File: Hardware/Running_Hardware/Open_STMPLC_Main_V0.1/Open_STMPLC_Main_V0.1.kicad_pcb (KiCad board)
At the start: 2 copper layers, 168.8 x 90 mm, 171 parts, among them J1 Conn_02x08_Odd_Even, J10 10144518-041802LF, J12 USB C, J13 RJ45_Hanrun_HR911105A_Horizon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, J2 USB C, J3 Conn_01x04, J4 TF-01A, J5 Conn_Coaxial, J6 Conn_Coaxial, J7 Simcard_Nano, J8 10144518-041802LF, J9 10144518-041802LF, Q1 DTC143Z, Q2 DTC143Z, Q3 DTC143Z, Q4 DTC143Z, Q5 DTC143Z, Q6 DTC143Z, Q7 DTC143Z, SW1 Switch_6x6, SW2 SW_SPDT, SW3 Switch_6x6, U1 STM32F407IGTx, U10 AP63205WU, U2 ADM2587E, U3 TPS3430WDRC, U4 CH340C, U5 AMS1117-3.3, U6 W25Q64JVSSIQ, U7 LAN8720A, U8 EC200U, U9 AP63200WU, Y1 48MHz, Y2 32.768kHz, Y3 25MHz

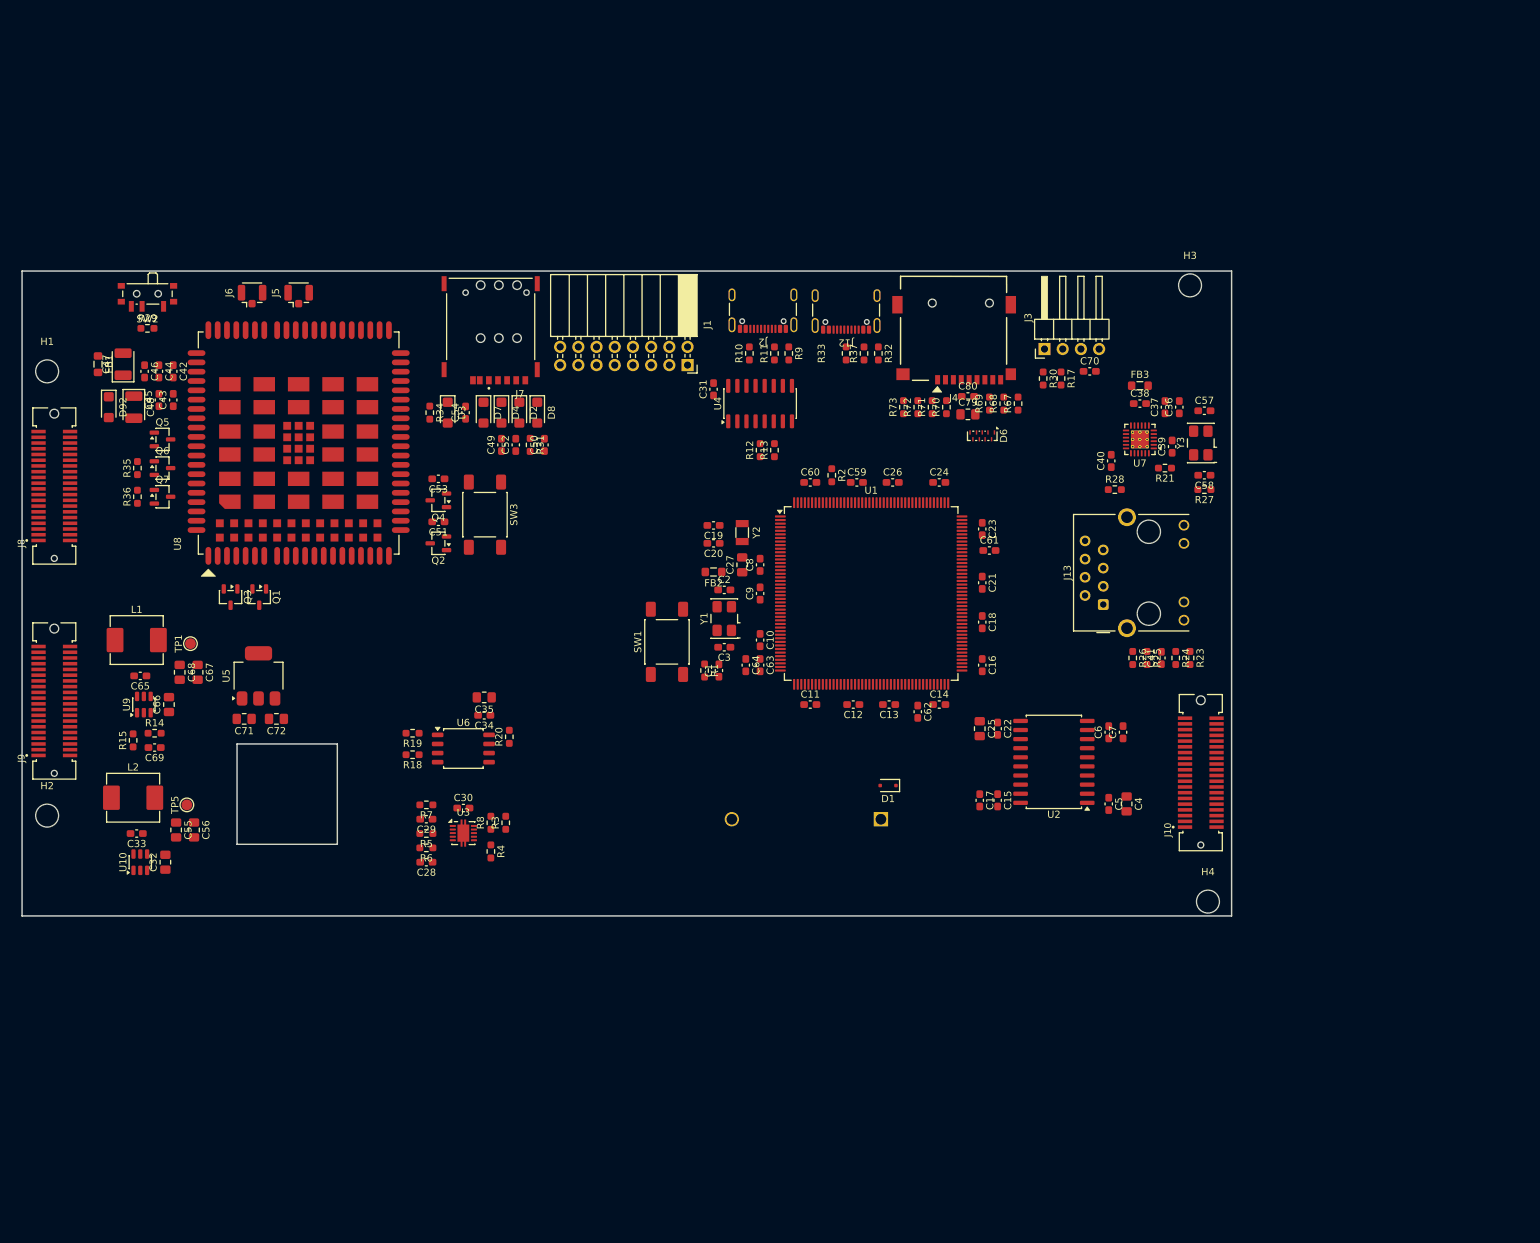
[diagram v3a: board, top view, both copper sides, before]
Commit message: Layer stack up main PCB and pin mapping
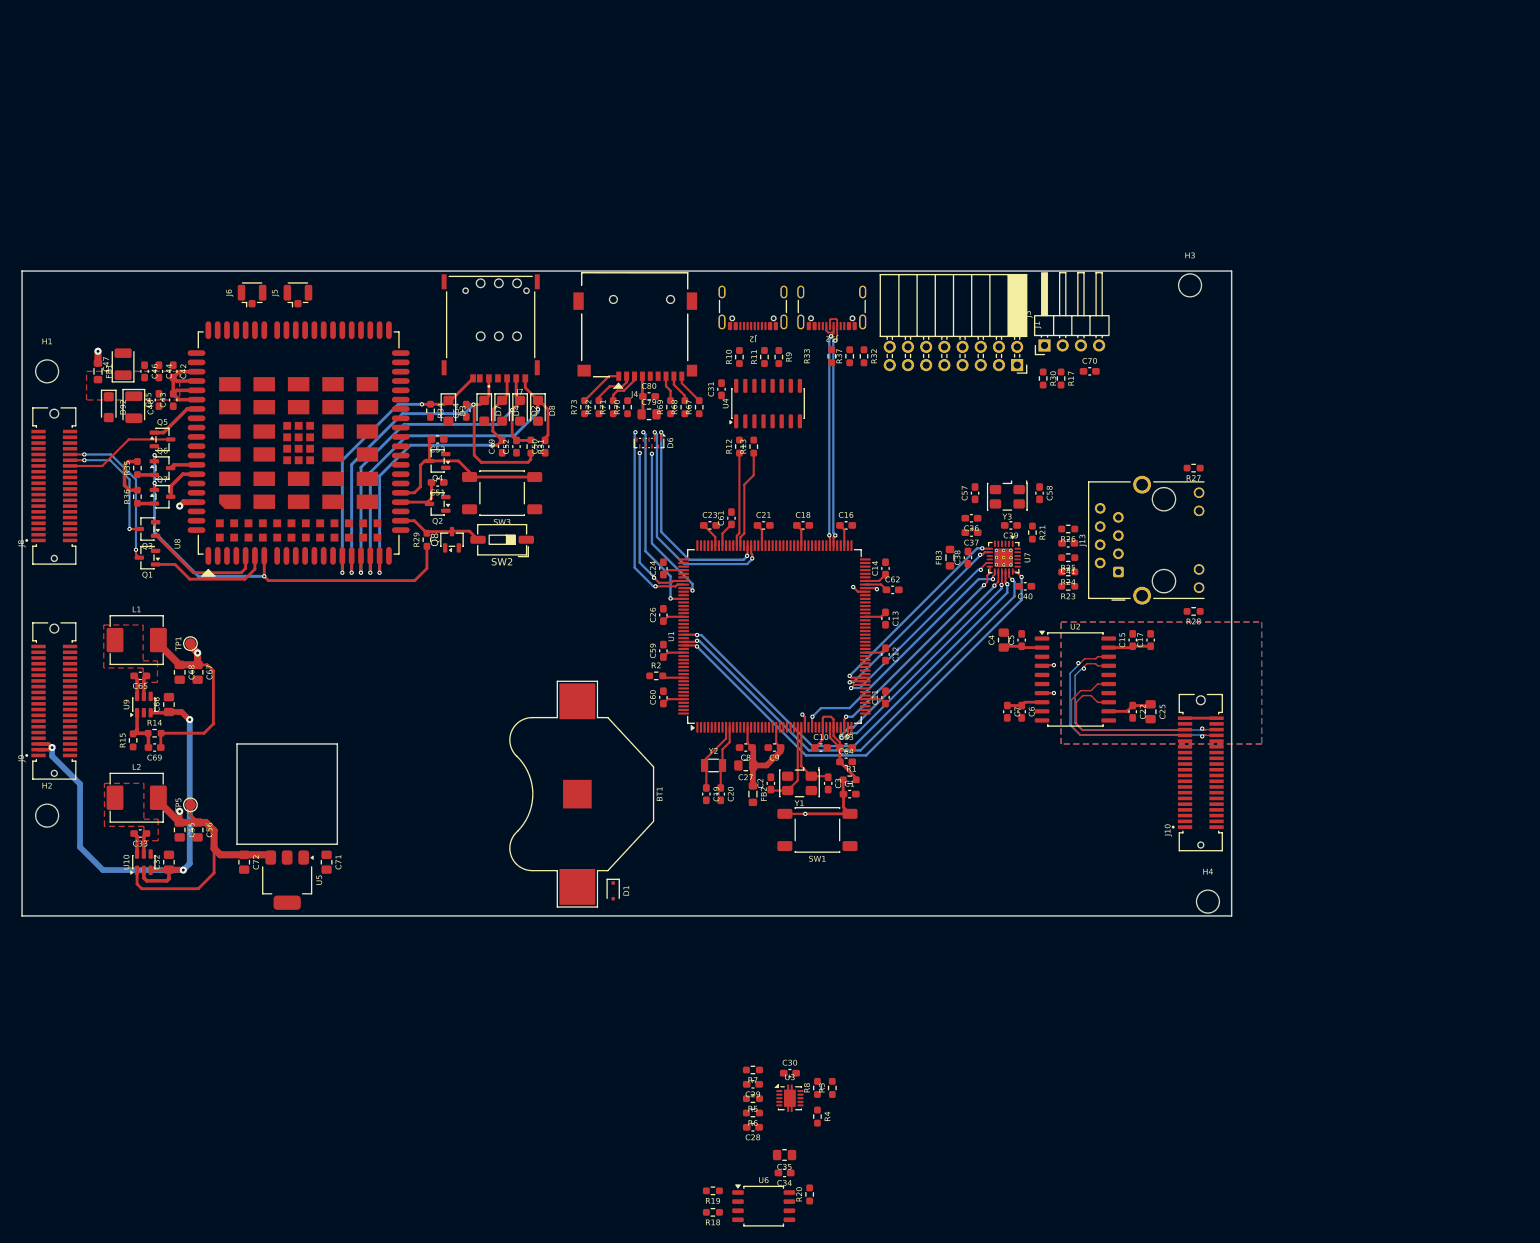
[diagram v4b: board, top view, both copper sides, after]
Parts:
- added Q8: DTC143Z, Package_TO_SOT_SMD:SOT-23-3, F.Cu at (110.0, 87.5)
- BT1: footprint Battery:BatteryHolder_MYOUNG_BS-07-A1BJ001_CR2032 -> Battery:BatteryHolder_Multicomp_BC-2001_1x2032; moved to F.Cu
- SW2: value SW_SPDT -> SW_DIP_x01; footprint Button_Switch_SMD:SW_SPDT_PCM12 -> Button_Switch_SMD:SW_DIP_SPSTx01_Slide_6.7x4.1mm_W6.73mm_P2.54mm_LowProfile_JPin
- moved C34 76.4 mm to (156.4, 175.9)
- moved C35 76.4 mm to (156.4, 173.4)
- moved R18 76.4 mm to (146.4, 181.4)
- moved R19 76.4 mm to (146.4, 178.4)
- moved R20 76.4 mm to (159.9, 178.9)
- moved U6 76.4 mm to (153.5, 180.5)
- moved SW2 60.1 mm to (117.0, 87.5)
- moved C28 58.7 mm to (152.0, 169.5)
- moved C29 58.7 mm to (152.0, 163.5)
- moved R4 58.7 mm to (161.0, 168.0)
- moved R5 58.7 mm to (152.0, 165.5)
- moved R6 58.7 mm to (152.0, 167.5)
- moved R7 58.7 mm to (152.0, 161.5)
- moved R8 58.7 mm to (161.0, 164.0)
- moved C30 58.7 mm to (157.2, 161.9)
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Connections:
- net Net-(J13-RD+) renamed /Ethernet/RD+
- net Net-(J13-RD-) renamed /Ethernet/RD-
- net Net-(J13-TD+) renamed /Ethernet/TD+
- net Net-(J13-TD-) renamed /Ethernet/TD-
- R12 pad 1: /Microcontroller/STM_RX -> /Microcontroller/DEBUG_RX
- R13 pad 1: /Microcontroller/STM_TX -> /Microcontroller/DEBUG_TX
- R29 pad 2: Net-(SW2-A) -> Net-(Q8-C)
- SW2 pad 1: Net-(SW2-A) -> GND
- SW2 pad 2: Net-(SW2-B) -> Net-(Q8-C)
- U1 pad 115: unconnected-(U1-PC6-Pad115) -> /Microcontroller/EX_UART_TX
- U1 pad 116: unconnected-(U1-PC7-Pad116) -> /Microcontroller/EX_UART_RX
- U1 pad 120: unconnected-(U1-PA9-Pad120) -> /Microcontroller/DEBUG_TX
- U1 pad 121: unconnected-(U1-PA10-Pad121) -> /Microcontroller/DEBUG_RX
- U1 pad 122: unconnected-(U1-PA11-Pad122) -> /GSM_Module/GSM_DN
- U1 pad 123: unconnected-(U1-PA12-Pad123) -> /GSM_Module/GSM_DP
- U1 pad 147: unconnected-(U1-PD5-Pad147) -> /GSM_Module/SIM_RX
- U1 pad 150: unconnected-(U1-PD6-Pad150) -> /GSM_Module/SIM_TX
- U1 pad 43: unconnected-(U1-PH2-Pad43) -> /Ethernet/ETH_~{RST}
- U1 pad 79: unconnected-(U1-PB10-Pad79) -> /MODBUS/RS485_TXD
- U1 pad 80: unconnected-(U1-PB11-Pad80) -> /MODBUS/RS485_RXD
- U1 pad 94: unconnected-(U1-PB14-Pad94) -> /Microcontroller/STM_DN
- U1 pad 95: unconnected-(U1-PB15-Pad95) -> /Microcontroller/STM_DP
- U8 pad 115: Net-(SW2-B) -> Net-(Q8-C)
- U9 pad 2: +24V -> /B2B_Connector/3V8_EN
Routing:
- net +5V: track 0.00 -> 87.7 mm, vias 0 -> 2
- net +3V8: track 0.00 -> 85.7 mm, vias 0 -> 2
- net /Microcontroller/3V3_MCU: track 0.00 -> 73.7 mm
- net +24V: track 0.00 -> 73.4 mm, vias 0 -> 3
- net /Ethernet/ETH_TXD1: track 0.00 -> 67.3 mm, vias 0 -> 2
- net /Ethernet/ETH_TXD0: track 0.00 -> 65.3 mm, vias 0 -> 2
- net /Ethernet/ETH_TXEN: track 0.00 -> 63.5 mm, vias 0 -> 2
- net /GSM_Module/USIM_VDD: track 0.00 -> 60.5 mm, vias 0 -> 2
- net +1V8: track 0.00 -> 60.0 mm, vias 0 -> 3
- net /GSM_Module/USIM_CLK: track 0.00 -> 55.1 mm, vias 0 -> 2
- net /GSM_Module/USIM_DATA: track 0.00 -> 53.1 mm, vias 0 -> 2
- net /GSM_Module/USIM_RST: track 0.00 -> 45.0 mm, vias 0 -> 2
- net /GSM_Module/USIM_DET: track 0.00 -> 41.0 mm, vias 0 -> 2
- net /MODBUS/RS485_TXD: track 0.00 -> 37.7 mm, vias 0 -> 2
- net /SD_DAT0: track 0.00 -> 36.5 mm, vias 0 -> 2
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- added copper zone on B.Cu, net GND_MODBUS
- added copper zone on F.Cu, net GND_MODBUS
- added copper zone on In1.Cu, net GND_MODBUS
- added copper zone on In2.Cu, net GND_MODBUS
- added copper zone on F.Cu, net Net-(D92-A1)
- added copper zone on F.Cu, net Net-(U10-SW)
- added copper zone on F.Cu, net Net-(U9-SW)
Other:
- copper layers 2 -> 4

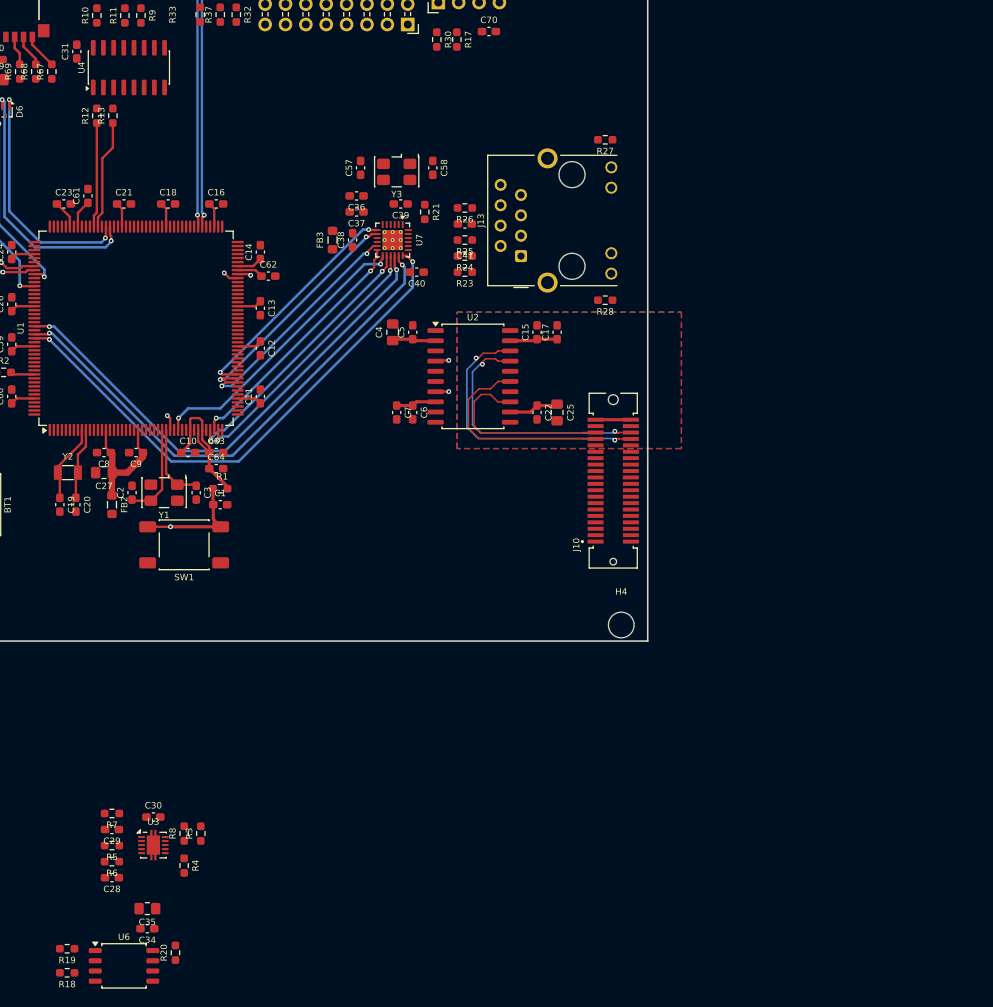
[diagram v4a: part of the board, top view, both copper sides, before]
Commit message: MCU pin mapping
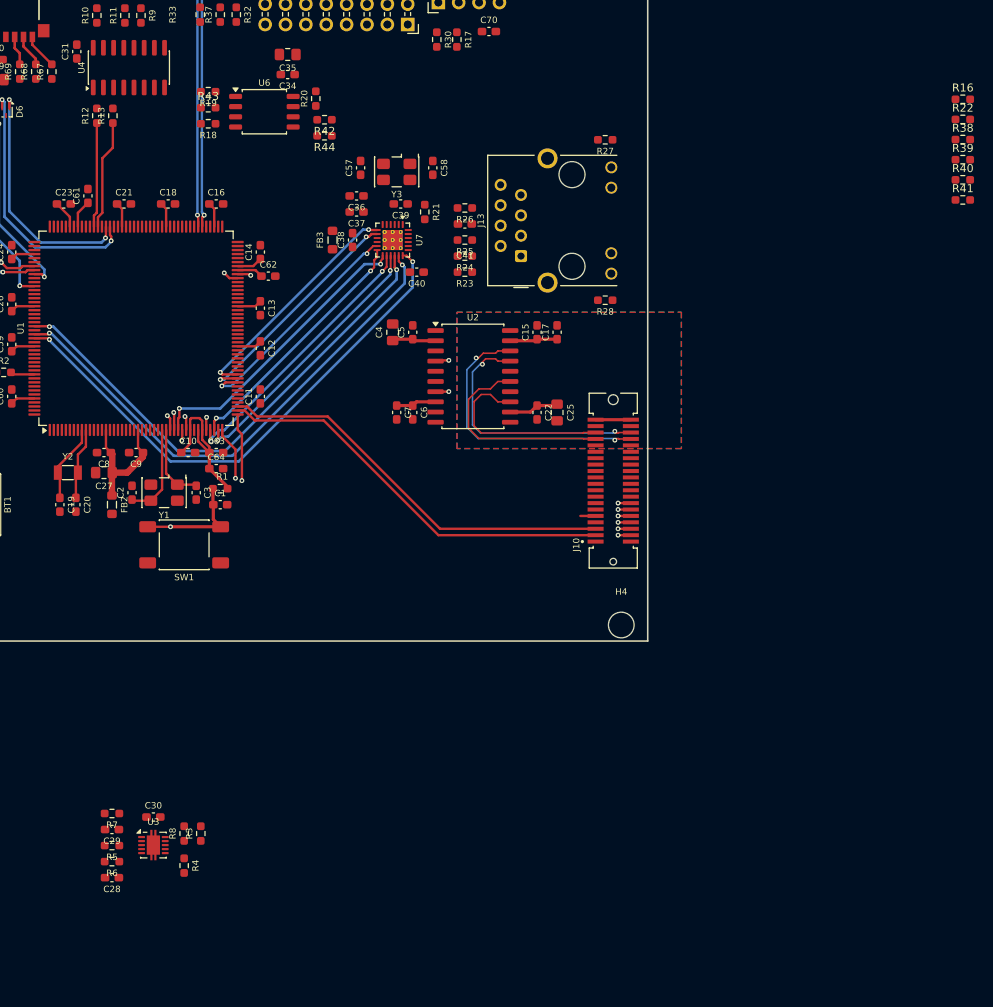
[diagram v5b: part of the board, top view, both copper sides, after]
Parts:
- added R16: 0R, Resistor_SMD:R_0603_1608Metric_Pad0.98x0.95mm_HandSolder, F.Cu at (258.1, 72.5)
- added R22: 0R, Resistor_SMD:R_0603_1608Metric_Pad0.98x0.95mm_HandSolder, F.Cu at (258.1, 75.0)
- added R38: 0R, Resistor_SMD:R_0603_1608Metric_Pad0.98x0.95mm_HandSolder, F.Cu at (258.1, 77.5)
- added R39: 0R, Resistor_SMD:R_0603_1608Metric_Pad0.98x0.95mm_HandSolder, F.Cu at (258.1, 80.0)
- added R40: 0R, Resistor_SMD:R_0603_1608Metric_Pad0.98x0.95mm_HandSolder, F.Cu at (258.1, 82.5)
- added R41: 0R, Resistor_SMD:R_0603_1608Metric_Pad0.98x0.95mm_HandSolder, F.Cu at (258.1, 85.0)
- added R42: 0R, Resistor_SMD:R_0603_1608Metric_Pad0.98x0.95mm_HandSolder, F.Cu at (178.5, 75.0)
- added R43: 0R, Resistor_SMD:R_0603_1608Metric_Pad0.98x0.95mm_HandSolder, F.Cu at (164.0, 73.5)
- added R44: 0R, Resistor_SMD:R_0603_1608Metric_Pad0.98x0.95mm_HandSolder, F.Cu at (178.5, 77.0)
- moved R19 108.3 mm to (164.0, 71.5)
- moved C34 107.9 mm to (173.9, 69.4)
- moved C35 107.9 mm to (173.9, 66.9)
- moved R20 107.9 mm to (177.4, 72.4)
- moved U6 107.9 mm to (171.0, 74.0)
- moved R18 107.3 mm to (164.0, 75.5)
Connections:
- U1 pad 132: unconnected-(U1-PI1-Pad132) -> /Microcontroller/SPI1_CLK
- U1 pad 133: unconnected-(U1-PI2-Pad133) -> /Microcontroller/SPI1_MISO
- U1 pad 134: unconnected-(U1-PI3-Pad134) -> /Microcontroller/SPI1_MOSI
- U1 pad 161: unconnected-(U1-PB3-Pad161) -> /Microcontroller/SPI1_CLK
- U1 pad 162: unconnected-(U1-PB4-Pad162) -> /Microcontroller/SPI1_MISO
- U1 pad 163: unconnected-(U1-PB5-Pad163) -> /Microcontroller/SPI1_MOSI
- U1 pad 32: unconnected-(U1-PC0-Pad32) -> /B2B_Connector/DIG_OUT_~{FAULT}_8
- U1 pad 34: unconnected-(U1-PC2-Pad34) -> /B2B_Connector/DIG_OUT_DIAG_8
- U1 pad 35: unconnected-(U1-PC3-Pad35) -> /B2B_Connector/DIG_OUT_8
- U1 pad 40: unconnected-(U1-PA0-Pad40) -> /B2B_Connector/DIG_OUT_~{FAULT}_5
- U1 pad 44: unconnected-(U1-PH3-Pad44) -> /B2B_Connector/DIG_OUT_DIAG_5
- U1 pad 45: unconnected-(U1-PH4-Pad45) -> /B2B_Connector/DIG_OUT_5
- U1 pad 46: unconnected-(U1-PH5-Pad46) -> /B2B_Connector/DIG_OUT_~{FAULT}_7
- U1 pad 47: unconnected-(U1-PA3-Pad47) -> /B2B_Connector/DIG_OUT_DIAG_7
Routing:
- net /B2B_Connector/DIG_OUT_~{FAULT}_8: track 0.00 -> 73.9 mm, vias 0 -> 2
- net /B2B_Connector/DIG_OUT_8: track 0.00 -> 71.0 mm, vias 0 -> 2
- net /B2B_Connector/DIG_OUT_~{FAULT}_5: track 0.00 -> 69.2 mm, vias 0 -> 2
- net /B2B_Connector/DIG_OUT_DIAG_8: track 0.00 -> 68.5 mm, vias 0 -> 2
- net /B2B_Connector/DIG_OUT_5: track 0.00 -> 64.6 mm, vias 0 -> 2
- net /B2B_Connector/DIG_OUT_DIAG_5: track 0.00 -> 64.2 mm, vias 0 -> 2
- net /B2B_Connector/DIG_OUT_~{FAULT}_7: track 0.00 -> 51.1 mm
- net /B2B_Connector/DIG_OUT_DIAG_7: track 0.00 -> 50.9 mm
- net /Microcontroller/3V3_MCU: track 73.7 -> 70.6 mm
- net /B2B_Connector/DIG_OUT_~{FAULT}_6: track 0.00 -> 1.90 mm
- net /Ethernet/ETH_MDC: track 35.8 -> 36.5 mm
